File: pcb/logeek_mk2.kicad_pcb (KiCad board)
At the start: 2 copper layers, 68.6 x 53.3 mm, 141 parts, among them P1 Power, P10 XH2.54-2P RA, P11 BARREL_JACK, P12 USB_B, P13 DC3 5x2, P14 Power, P15 Analog, P16 Digital, P17 Digital, P2 Analog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

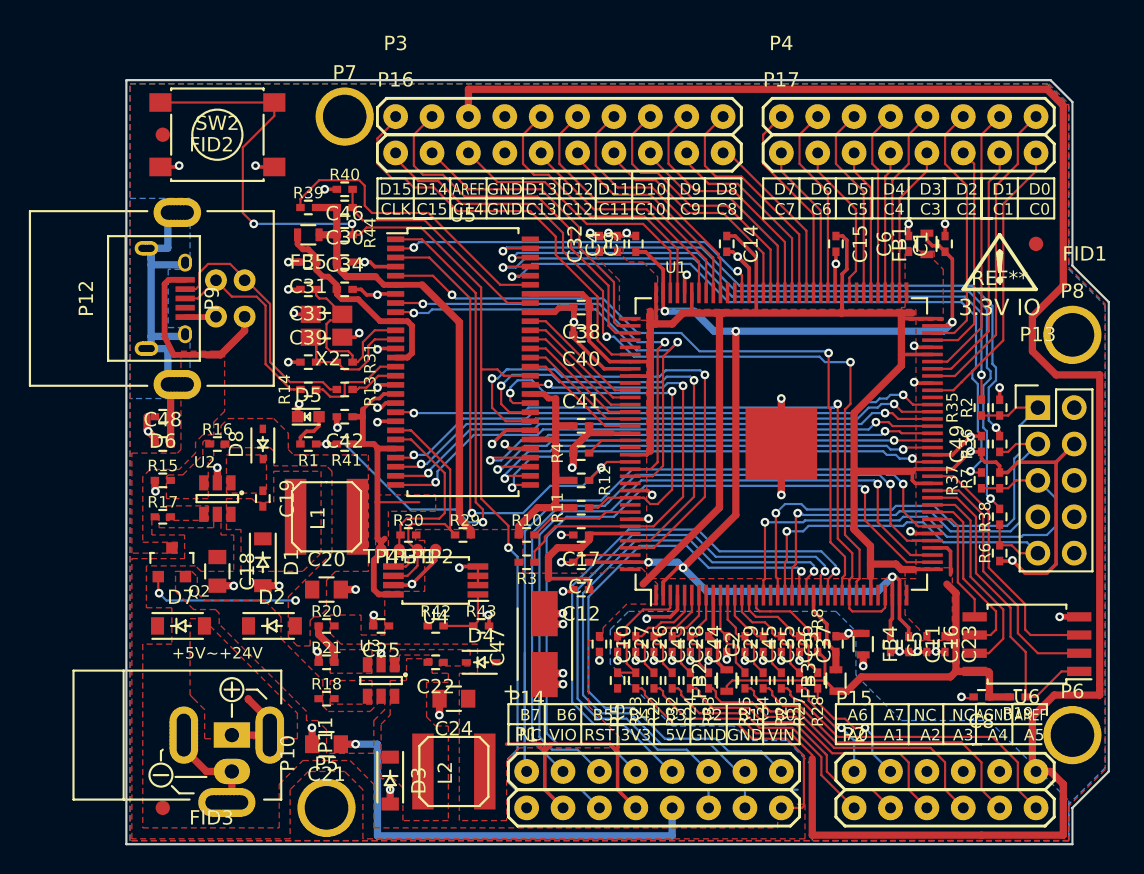
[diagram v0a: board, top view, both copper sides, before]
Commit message: Fine-tune copper and silkscreen. Add a fuse on USB power input.
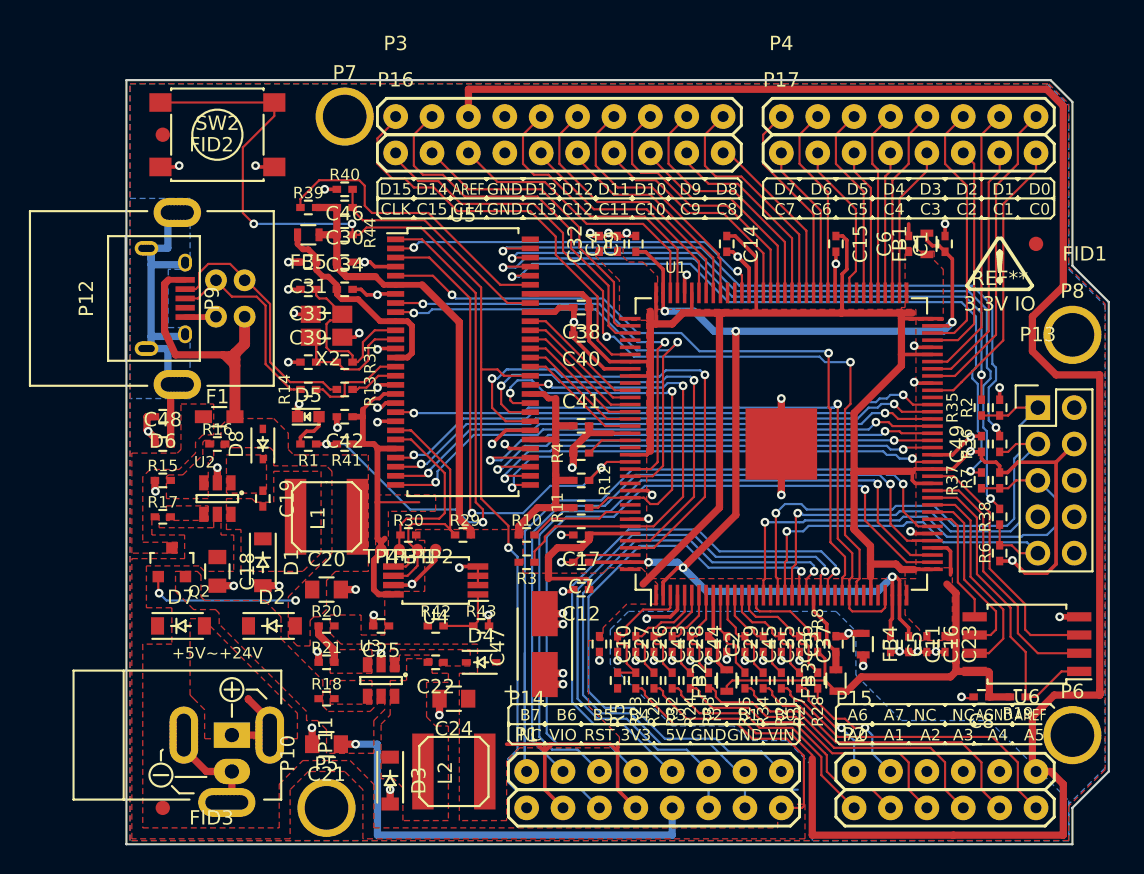
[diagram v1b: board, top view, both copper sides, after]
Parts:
- added F1: 500mA, Resistors_SMD:R_0603_HandSoldering, F.Cu at (117.5, 96.5)
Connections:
- Q2 pad 3: /USBPWR -> Net-(F1-Pad2)
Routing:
- net /USBPWR: track 13.3 -> 19.6 mm
- net GNDD: track 172.6 -> 173.1 mm, vias 64 -> 63
- net /AREF: track 141.0 -> 141.5 mm
- added copper zone on F.Cu, net Net-(F1-Pad2)
- removed copper zone on F.Cu, net /USBPWR

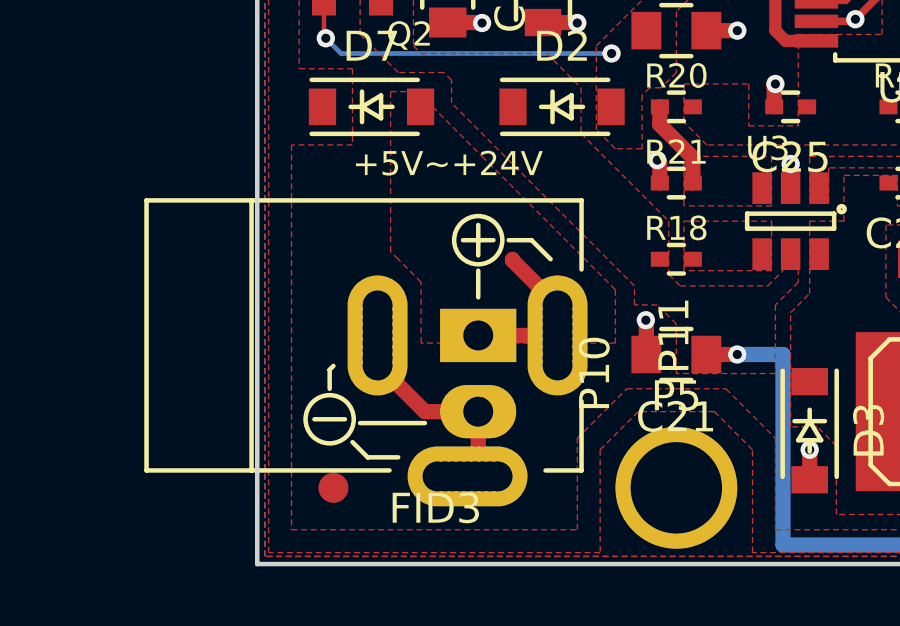
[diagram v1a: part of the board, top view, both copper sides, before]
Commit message: Power input socket changed to 5.08mm terminal.
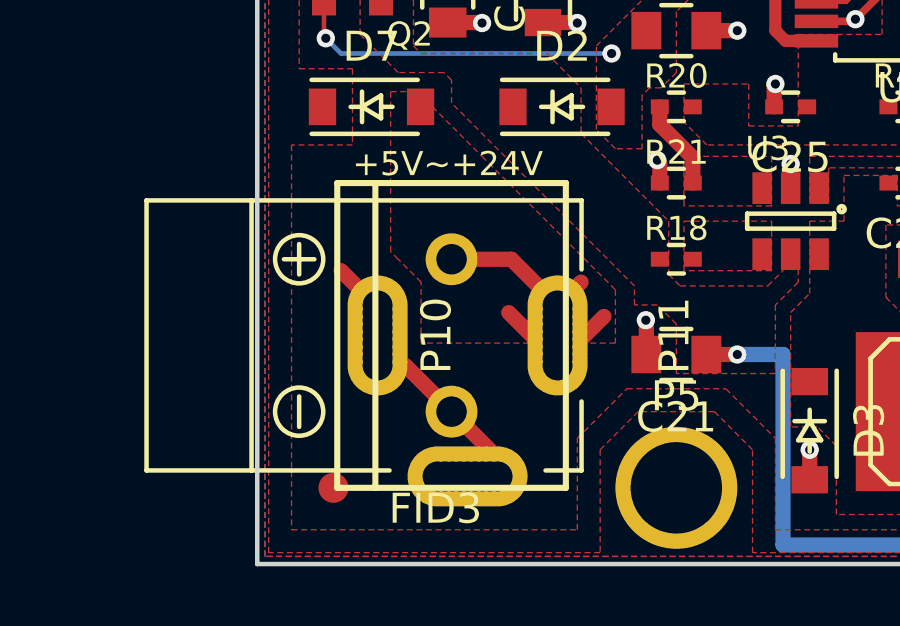
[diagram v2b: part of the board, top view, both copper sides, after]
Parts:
- P10: footprint Logeek_MK2:PINHEAD1-2 -> Logeek_MK2:DG301_2P_5.08mm_Straight
- moved P10 1.55 mm to (117.5, 118.7)
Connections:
- net /A8 renamed Net-(P15-Pad3)
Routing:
- net /VIN: track 6.81 -> 14.0 mm
- net GNDD: track 173.1 -> 177.2 mm

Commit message: C14,C15,CLK and GND pins changed.
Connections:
- P16 pad 1: /EXTCLK -> GNDD
- P16 pad 2: /C15 -> /EXTCLK
- P16 pad 3: /C14 -> /C15
- P16 pad 4: GNDD -> /C14
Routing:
- net /D14: track 26.3 -> 23.6 mm
- net /C15: track 21.3 -> 18.7 mm
- net /D15: track 29.5 -> 27.2 mm
- net /C14: track 19.8 -> 17.8 mm
- net /EXTCLK: track 57.4 -> 55.5 mm

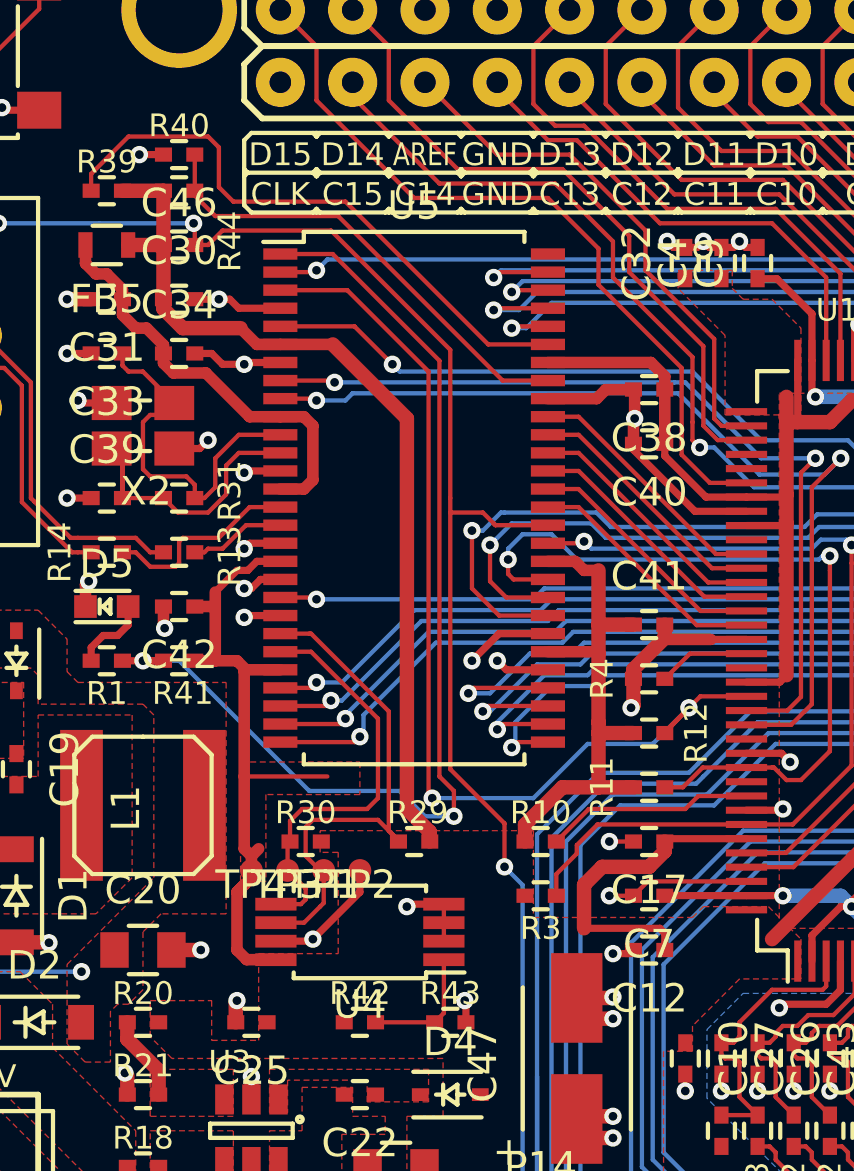
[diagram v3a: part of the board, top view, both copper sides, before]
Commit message: Fine-tuned silk art. Gerber generated.
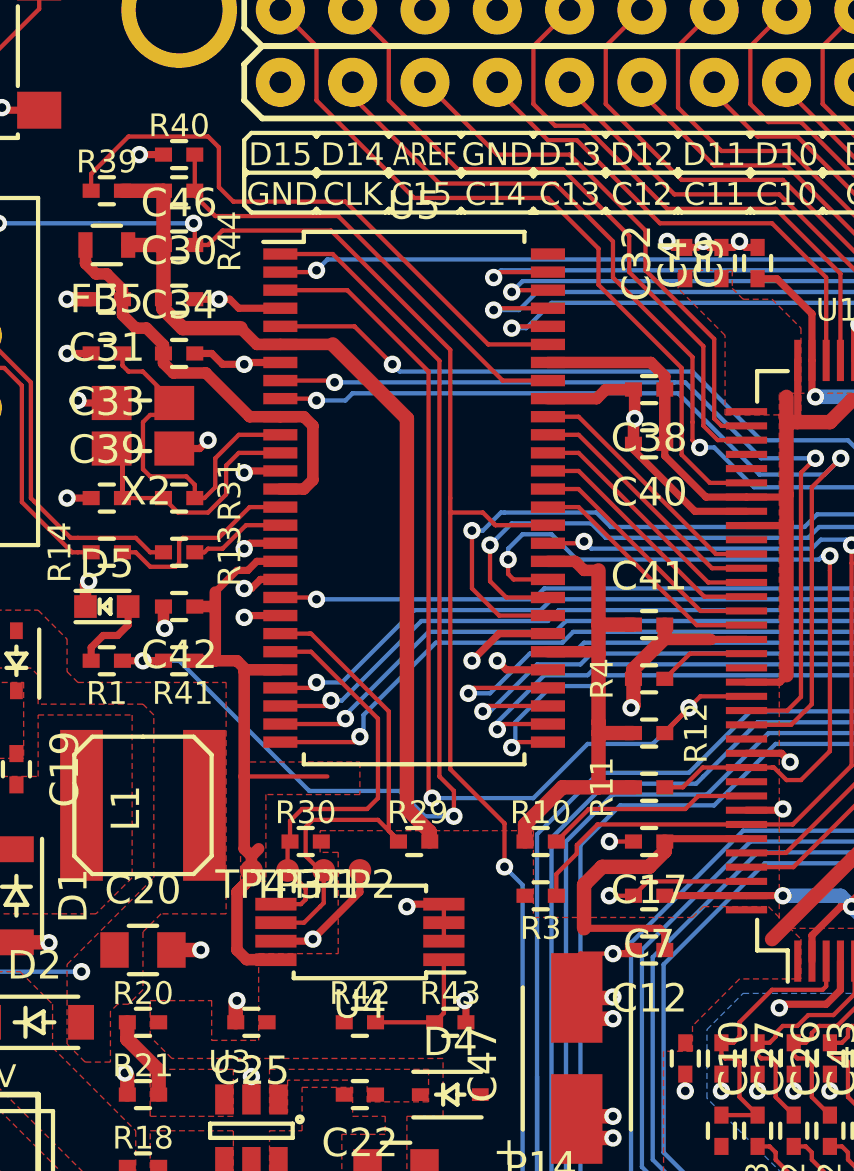
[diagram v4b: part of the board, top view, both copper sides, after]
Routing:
- net GNDD: track 177.6 -> 180.4 mm

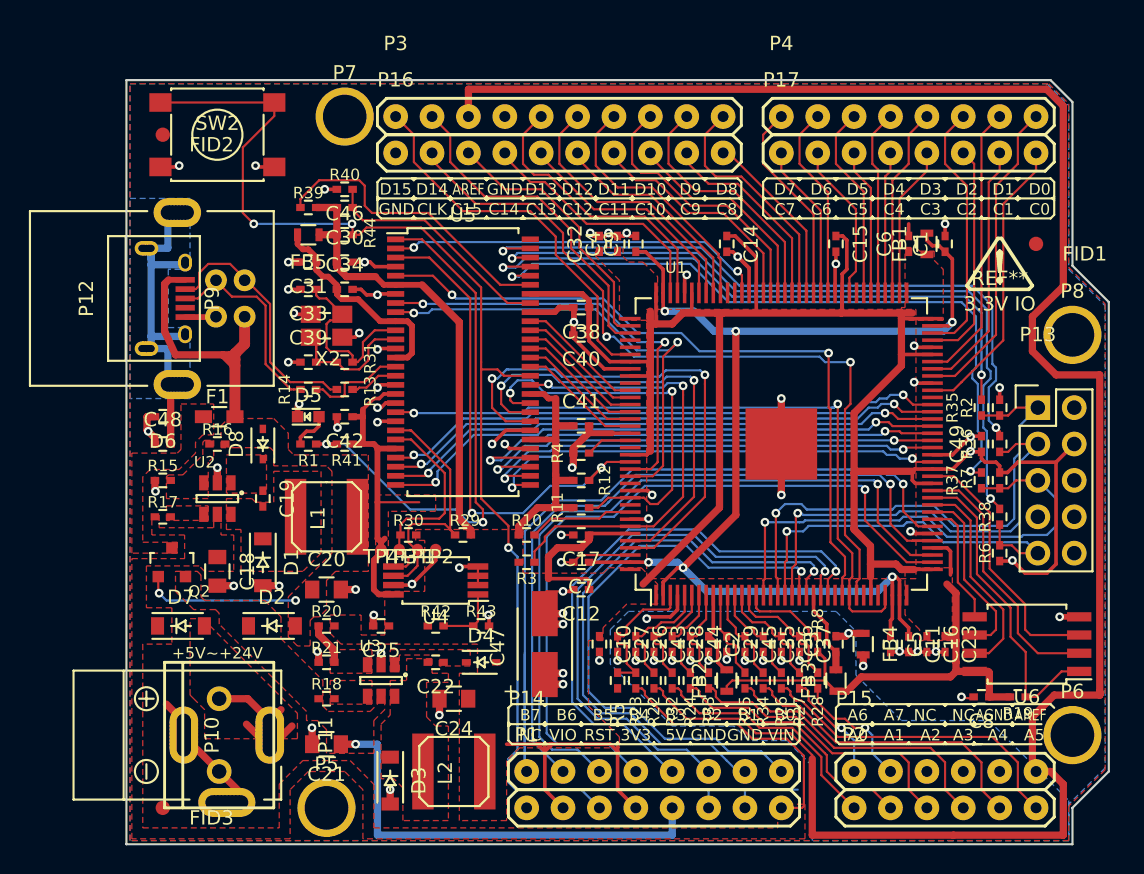
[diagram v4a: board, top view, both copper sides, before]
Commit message: Power supplies redesigned.
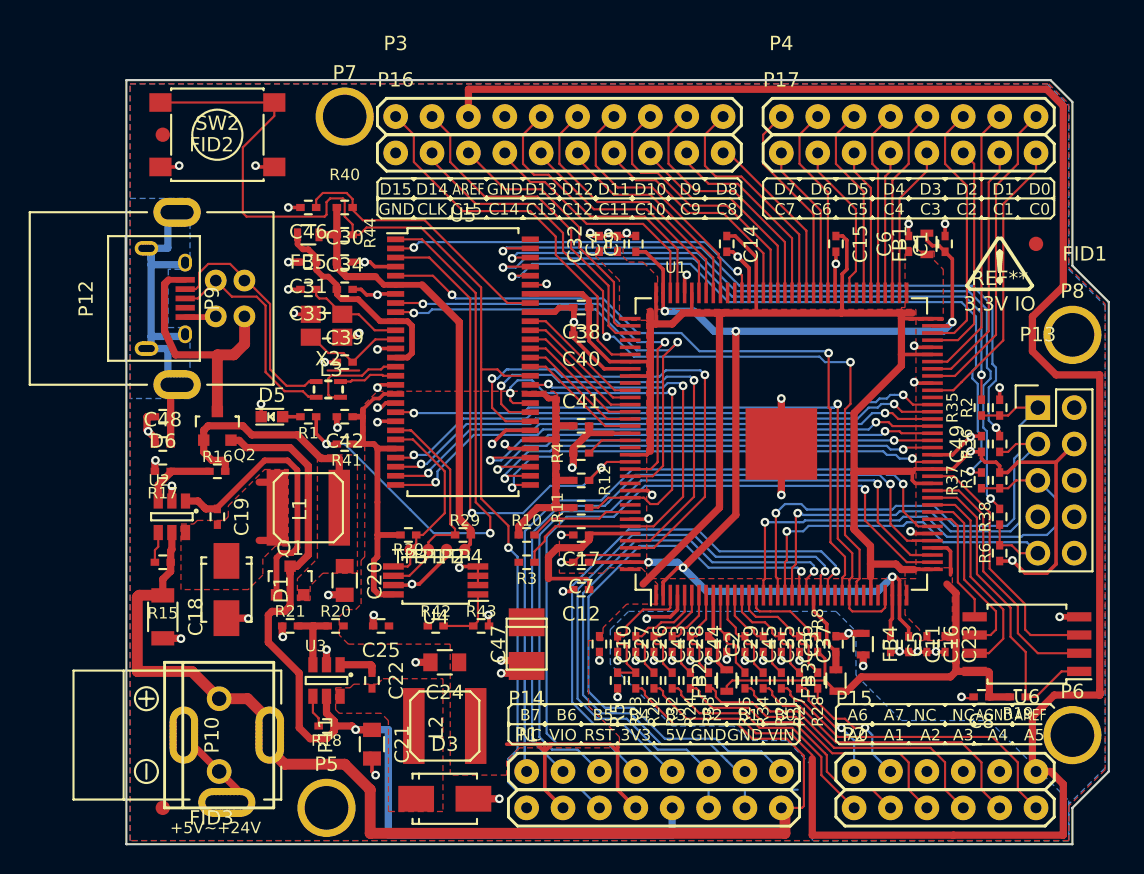
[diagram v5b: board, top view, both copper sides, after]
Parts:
- removed D2, D7: 1N5819WS, Diodes_SMD:SOD-123
- removed D4, D8: 1N4148WS, Diodes_SMD:SOD-323
- removed F1: 500mA, Resistors_SMD:R_0603_HandSoldering
- removed R13, R14: 22, Resistors_SMD:R_0402_HandSoldering
- removed R31: 1000k, Resistors_SMD:R_0402_HandSoldering
- removed R39: 10k, Resistors_SMD:R_0402_HandSoldering
- added L3: DLW21SN900SQ2, Logeek_MK2:CommonModeChoke_0805, F.Cu at (125.1, 94.6)
- added Q1: SI2302CDS, Housings_SOT-23_SOT-143_TSOT-6:SOT-23, F.Cu at (122.4, 108.0)
- C18: footprint Capacitors_SMD:C_0805 -> Capacitors_SMD:C_1206
- C47: footprint Logeek_MK2:TantalC_SizeB_EIA-3528_HandSoldering -> Capacitors_Tantalum_SMD:TantalC_SizeT_EIA-3528
- D1, D3: value 1N5819WS -> B230A; footprint Diodes_SMD:SOD-123 -> Diodes_SMD:Diode-SMA_Standard
- D5: value LED TRUE GREEN -> LED GREEN
- P10: value XH2.54-2P RA -> DG301-2P 5.08mm
- moved Q2 10.0 mm to (117.3, 97.2)
- moved TP4 5.84 mm to (134.6, 105.8)
- moved C18 4.96 mm to (113.5, 110.5)
- moved C22 4.62 mm to (128.1, 114.9), turned to 270 degrees
- moved D3 4.02 mm to (133.2, 123.2), turned to 0 degrees
- moved U3 3.81 mm to (125.0, 114.9)
- moved R21 3.59 mm to (122.4, 111.1)
- moved C19 3.42 mm to (117.3, 103.5)
- moved U2 3.42 mm to (114.2, 103.5)
- moved L2 3.24 mm to (133.2, 118.1)
- moved R15 3.18 mm to (113.5, 106.7), turned to 180 degrees
- moved C21 3.17 mm to (128.1, 119.4), turned to 270 degrees
- moved D1 3.17 mm to (118.0, 108.6)
- moved C46 2.84 mm to (123.7, 81.9)
- moved C24 2.62 mm to (133.2, 113.7)
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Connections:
- C18 pad 1: /VIN_SAFE -> VIN
- P1 pad 8: /VIN_SAFE -> VIN
- P10 pad 1: /VIN -> VIN
- P11 pad 1: /VIN -> VIN
- Q2 pad 3: Net-(F1-Pad2) -> /USBPWR
- R15 pad 1: /VIN_SAFE -> VIN
- R23 pad 2: /VIN_SAFE -> VIN
- U2 pad 5: /VIN_SAFE -> VIN
- U5 pad 51: /WAKEUP -> GNDD
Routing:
- net VIN: track 0.00 -> 87.6 mm
- net +5V: track 31.4 -> 67.6 mm
- net /WAKEUP: track 21.0 -> 0.00 mm
- net /5VBS: track 0.00 -> 19.5 mm
- net /VIN_SAFE: track 19.0 -> 0.00 mm
- net /VIN: track 14.0 -> 0.00 mm
- net /5VSW: track 0.00 -> 6.60 mm
- net /XTALO: track 13.5 -> 8.23 mm
- net /5VBAK: track 12.9 -> 17.9 mm, vias 2 -> 0
- net /5VFB: track 0.15 -> 5.14 mm
- net +3V3: track 288.6 -> 284.2 mm, vias 4 -> 2
- net /CPU_RESETn: track 16.5 -> 19.5 mm
- net /3VBS: track 0.00 -> 2.73 mm
- net /XTALI: track 11.0 -> 8.38 mm
- net /LEDEN: track 38.7 -> 41.3 mm
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- removed copper zone on F.Cu, net +5V
- removed copper zone on F.Cu, net /3VBS
- removed copper zone on F.Cu, net /3VEN
- removed copper zone on F.Cu, net /3VFB
- removed copper zone on F.Cu, net /5VBS
- removed copper zone on F.Cu, net /5VEN
- removed copper zone on F.Cu, net /5VFB
- removed copper zone on F.Cu, net /VIN
- removed copper zone on F.Cu, net /VIN_SAFE
- removed copper zone on F.Cu, net Net-(F1-Pad2)
